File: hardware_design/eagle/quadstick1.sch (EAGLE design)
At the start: 33 parts, among them J1 USB MICRO, U1 ATMEGA32U4-XUMU, Y1 16MHz KX-7

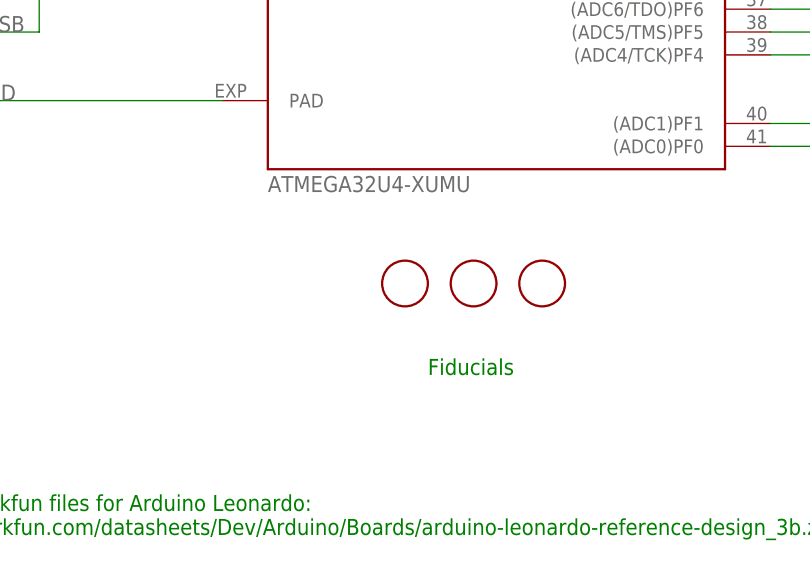
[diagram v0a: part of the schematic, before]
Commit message: added eagle layout
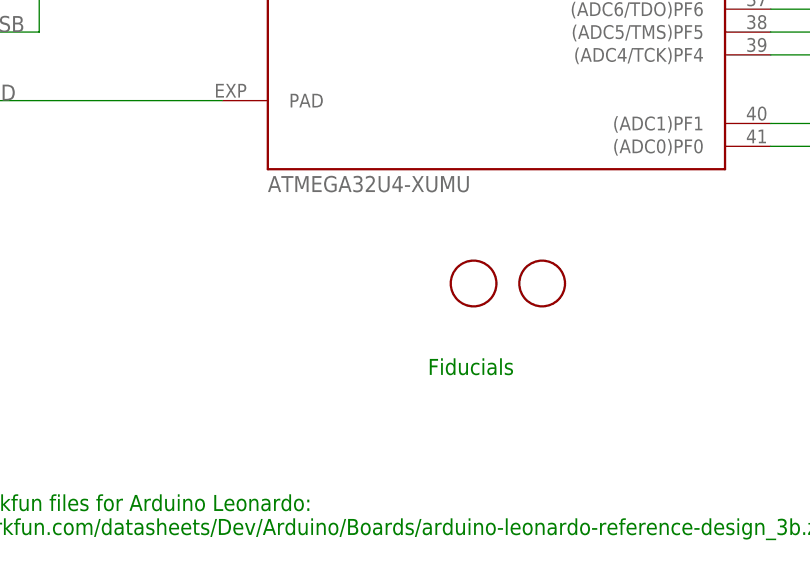
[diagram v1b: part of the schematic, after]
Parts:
- removed FID1: FIDUCIALMOUNT, SmartPrj:FIDUCIALMOUNT
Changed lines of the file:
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@@
 <?xml version="1.0" encoding="utf-8"?>
 <!DOCTYPE eagle SYSTEM "eagle.dtd">
-<eagle version="8.4.1">
+<eagle version="8.4.0">
 <drawing>
 <settings>
@@
 <part name="GND1" library="supply1" deviceset="GND" device="" value="3x2M_NM"/>
 <part name="GND12" library="supply1" deviceset="GND" device=""/>
-<part name="FID1" library="SmartPrj" deviceset="FIDUCIALMOUNT" device=""/>
 <part name="FID2" library="SmartPrj" deviceset="FIDUCIALMOUNT" device=""/>
 <part name="FID3" library="SmartPrj" deviceset="FIDUCIALMOUNT" device=""/>
@@
 <instance part="GND1" gate="1" x="-86.36" y="83.82" rot="R90"/>
 <instance part="GND12" gate="1" x="-137.16" y="96.52"/>
-<instance part="FID1" gate="G$1" x="-30.48" y="-48.26"/>
 <instance part="FID2" gate="G$1" x="-22.86" y="-48.26"/>
 <instance part="FID3" gate="G$1" x="-15.24" y="-48.26"/>
